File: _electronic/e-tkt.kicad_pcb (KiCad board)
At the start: 4 copper layers, 99.6 x 76.2 mm, 110 parts

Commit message: pcb v1 to production
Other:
- board text added: "2022/09/23"
- board text removed: "2022/09/21"
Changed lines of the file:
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@@
       (xy 149.352 -213.36)
     ) (layer "B.SilkS") (width 0.15) (fill solid))
-  (gr_line (start 144.379749 -162.052002) (end 145.27631 -162.052002) (layer "F.SilkS") (width 0.25))
-  (gr_circle (center 143.24431 -162.052002) (end 143.24431 -162.560002) (layer "F.SilkS") (width 0.25) (fill solid))
-  (gr_line (start 146.920232 -162.052002) (end 145.904232 -162.052002) (layer "F.SilkS") (width 0.25))
-  (gr_line (start 141.211827 -162.052002) (end 143.243976 -162.052002) (layer "F.SilkS") (width 0.25))
-  (gr_arc (start 142.73631 -163.068002) (mid 144.379784 -162.052002) (end 142.73631 -161.036002) (layer "F.SilkS") (width 0.25))
-  (gr_line (start 139.567905 -162.052002) (end 140.583905 -162.052002) (layer "F.SilkS") (width 0.25))
-  (gr_circle (center 146.412232 -162.052002) (end 146.412232 -163.187925) (layer "F.SilkS") (width 0.25) (fill none))
-  (gr_line (start 140.075905 -161.544002) (end 140.075905 -162.560002) (layer "F.SilkS") (width 0.25))
-  (gr_circle (center 140.075905 -162.052002) (end 140.075905 -163.187925) (layer "F.SilkS") (width 0.25) (fill none))
+  (gr_line (start 144.136437 -162.179) (end 145.032998 -162.179) (layer "F.SilkS") (width 0.25))
+  (gr_circle (center 143.000998 -162.179) (end 143.000998 -162.687) (layer "F.SilkS") (width 0.25) (fill solid))
+  (gr_line (start 146.67692 -162.179) (end 145.66092 -162.179) (layer "F.SilkS") (width 0.25))
+  (gr_line (start 140.968515 -162.179) (end 143.000664 -162.179) (layer "F.SilkS") (width 0.25))
+  (gr_arc (start 142.492998 -163.195) (mid 144.136474 -162.178997) (end 142.492998 -161.163) (layer "F.SilkS") (width 0.25))
+  (gr_line (start 139.324593 -162.179) (end 140.340593 -162.179) (layer "F.SilkS") (width 0.25))
+  (gr_circle (center 146.16892 -162.179) (end 146.16892 -163.314923) (layer "F.SilkS") (width 0.25) (fill none))
+  (gr_line (start 139.832593 -161.671) (end 139.832593 -162.687) (layer "F.SilkS") (width 0.25))
+  (gr_circle (center 139.832593 -162.179) (end 139.832593 -163.314923) (layer "F.SilkS") (width 0.25) (fill none))
   (gr_line (start 134.560258 -151.550617) (end 134.445168 -151.58932) (layer "Edge.Cuts") (width 0.02))
   (gr_line (start 131.831791 -178.139401) (end 131.785272 -178.251708) (layer "Edge.Cuts") (width 0.02))
@@
     (effects (font (size 2 2) (thickness 0.3)))
   )
-  (gr_text "2022/09/21" (at 139.7 -154.94) (layer "B.Mask")
+  (gr_text "2022/09/23" (at 139.7 -154.94) (layer "B.Mask")
     (effects (font (size 1.3 1.3) (thickness 0.3)) (justify right mirror))
   )

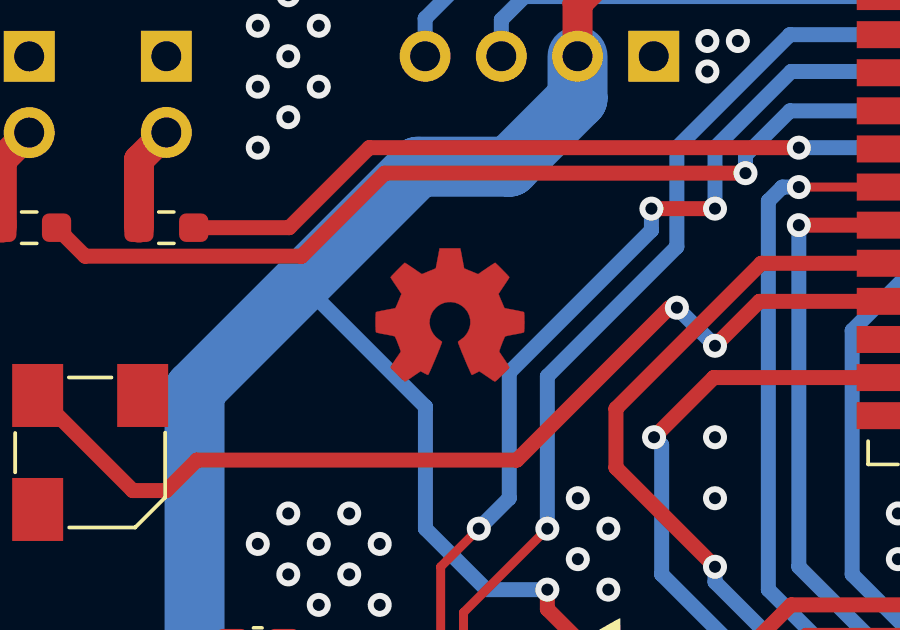
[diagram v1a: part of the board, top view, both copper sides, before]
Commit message: led resistor revision, b.o.m. and pcb anotation
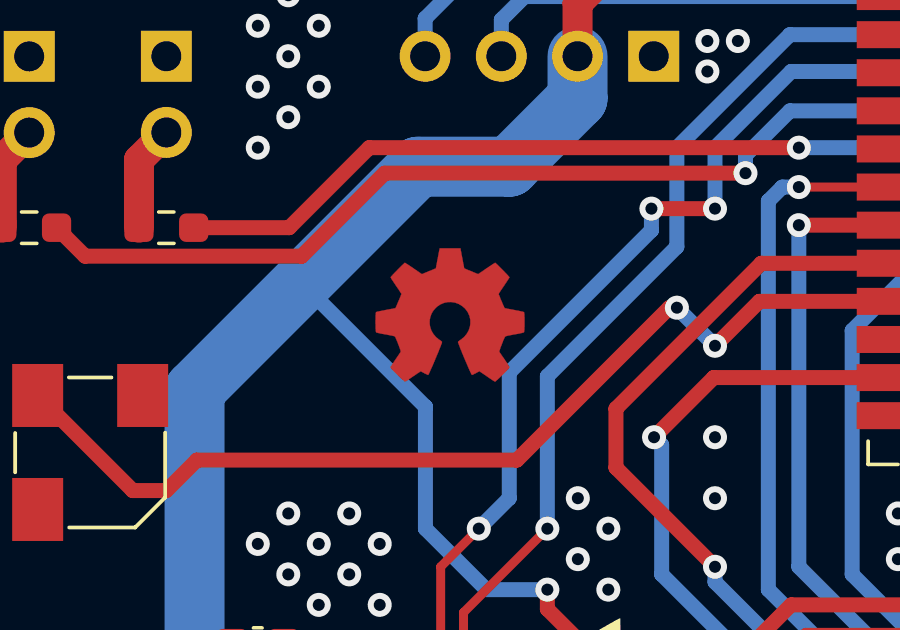
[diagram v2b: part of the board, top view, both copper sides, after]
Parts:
- C_POW_IN1, C_POW_IN2, C_POW_IN3: value 10uF 25V -> 22uF 25V
- R_AUTO1, R_AUTO2, R_DFU1, R_ENA1, R_HALL1, R_HALL2, R_SERVO1, R_SERVO2: value 10K (5%) -> 10K
- R_HALL3, R_NEMA1, R_NEMA2, R_RX1, R_SERVO3, R_TX1: value 27R -> 100R
- R_POW6, R_STP1, R_STP2, R_STP3, R_STP4: value 430R -> 5K1
- R_USB1, R_USB2: value 5.1K (10%) -> 5.1K
- R_USB3: value 100R -> 2K
- R_WIFI1: value 10K(5%) -> 10K

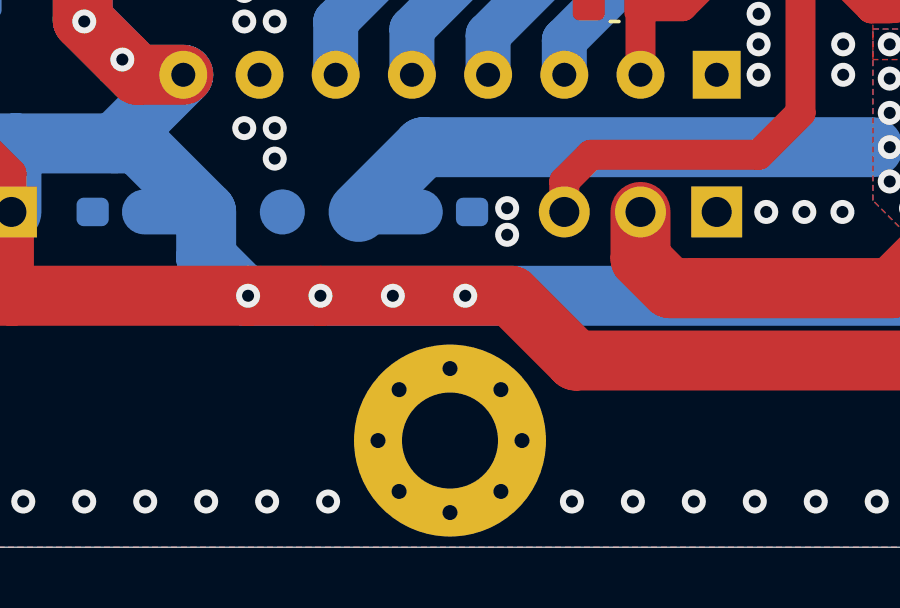
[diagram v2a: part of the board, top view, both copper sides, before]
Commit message: schematics and pcb cleanup
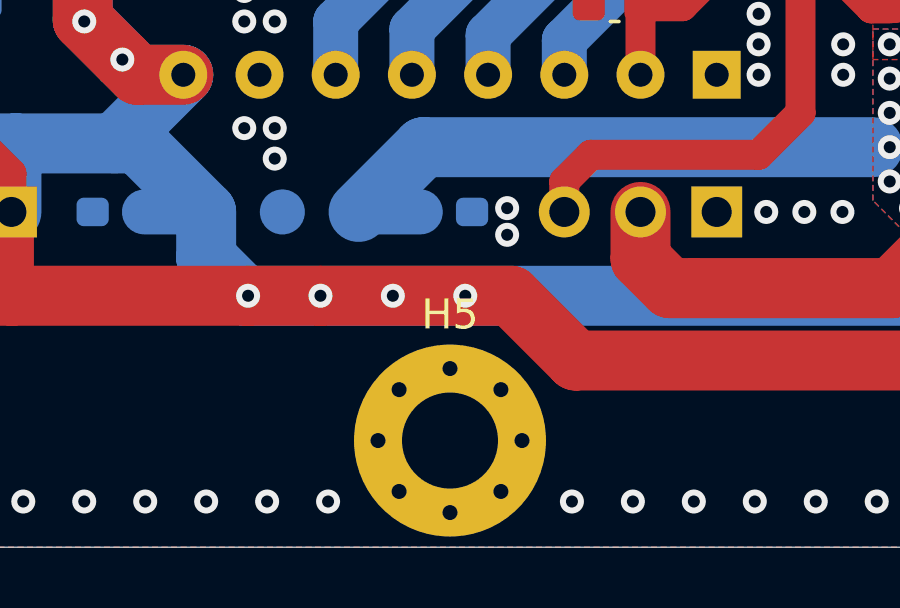
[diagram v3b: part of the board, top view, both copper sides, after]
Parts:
- removed C_POW_BST2: 0.33uF 50V, Capacitor_SMD:C_0603_1608Metric_Pad1.08x0.95mm_HandSolder
- removed C_POW_BST3: 0.1uF 50V, Capacitor_SMD:C_0603_1608Metric_Pad1.08x0.95mm_HandSolder
- removed H6: M3, MountingHole:MountingHole_3.2mm_M3_Pad_Via
- removed J_B_12v_1, J_B_6v_1, J_B_GND_1: TestPoint, TestPoint:TestPoint_Pad_D1.5mm
- added C_ALT6V_1: 0.33uF 50V, Capacitor_SMD:C_0603_1608Metric_Pad1.08x0.95mm_HandSolder, B.Cu at (167.3, -162.6)
- added C_ALT6V_2: 0.1uF 50V, Capacitor_SMD:C_0603_1608Metric_Pad1.08x0.95mm_HandSolder, B.Cu at (178.2, -162.6)
- added H5: M3, MountingHole:MountingHole_3.2mm_M3_Pad_Via, F.Cu at (178.3, -154.9)
- added J_12v_ALT6V1: TestPoint, TestPoint:TestPoint_Pad_D1.5mm, B.Cu at (170.2, -162.6)
- added J_6v_ALT6V1: TestPoint, TestPoint:TestPoint_Pad_D1.5mm, B.Cu at (175.3, -162.6)
- added J_GND_ALT6V1: TestPoint, TestPoint:TestPoint_Pad_D1.5mm, B.Cu at (172.7, -162.6)
- C_MCU2, C_POW2: value 22uF 12V 1mOhm -> 10uF 12V
- C_NEMA2, C_POW1, C_SER5, C_STP1: value 10uF 12V 5mOhm -> 10uF 12V
- C_POW_6V_FF1: value 82pF 100V -> 47pF 50V
- C_SER2, C_SER3: value 47pF 5V -> 47pF 50V
- R_USB1, R_USB2: value 5.1K -> 5K1
